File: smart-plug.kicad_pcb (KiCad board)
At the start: 2 copper layers, 58 x 53 mm, 24 parts, among them J1 Screw_Terminal_01x03, Q1 STGD5NB120SZ, Q2 BTA316B-600E, U1 ESP32-PICO-KIT, U2 SR086, U3 TPS560430X3F, U4 FODM3012

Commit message: rename project
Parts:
- D1: footprint ThinglerV05:ABS10A -> smart-plug:ABS10A
- F1: footprint ThinglerV05:Fuse -> smart-plug:Fuse
- L1: footprint ThinglerV05:ME3220 -> smart-plug:ME3220
- U1: footprint ThinglerV05:ESP32-PICO-KIT -> smart-plug:ESP32-PICO-KIT
- U4: footprint ThinglerV05:FODM3012 -> smart-plug:FODM3012
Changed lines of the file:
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@@
     (add_net "Net-(R8-Pad2)")
   )
-  (module ThinglerV05:FODM3012 (layer F.Cu)
+  (module smart-plug:FODM3012 (layer F.Cu)
     (at 168.5 70.25 180)
     (fp_text reference U4 (at 0 0) (layer F.SilkS)
@@
       (net 20 "Net-(R5-Pad1)"))
   )
-  (module ThinglerV05:ESP32-PICO-KIT (layer F.Cu)
+  (module smart-plug:ESP32-PICO-KIT (layer F.Cu)
     (at 145 86.75 90)
     (fp_text reference U1 (at 0 0 180) (layer F.SilkS)
@@
     )
   )
-  (module ThinglerV05:ME3220 (layer F.Cu)
+  (module smart-plug:ME3220 (layer F.Cu)
     (at 157.25 73)
     (fp_text reference L1 (at 0 2.75) (layer F.SilkS)
@@
     )
   )
-  (module ThinglerV05:ABS10A (layer F.Cu)
+  (module smart-plug:ABS10A (layer F.Cu)
     (at 138.5 66.25 90)
     (fp_text reference D1 (at 0 0 180) (layer F.SilkS)
@@
       (net 13 "Net-(D1-Pad4)"))
   )
-  (module ThinglerV05:Fuse (layer F.Cu)
+  (module smart-plug:Fuse (layer F.Cu)
     (at 131.75 66.25 180)
     (descr "Littelfuse, resettable fuse, PTC, polyswitch LVR100, Ih 1A http://www.littelfuse.com/~/media/electronics/datasheets/resettable_ptcs/littelfuse_ptc_lvr_catalog_datasheet.pdf.pdf")

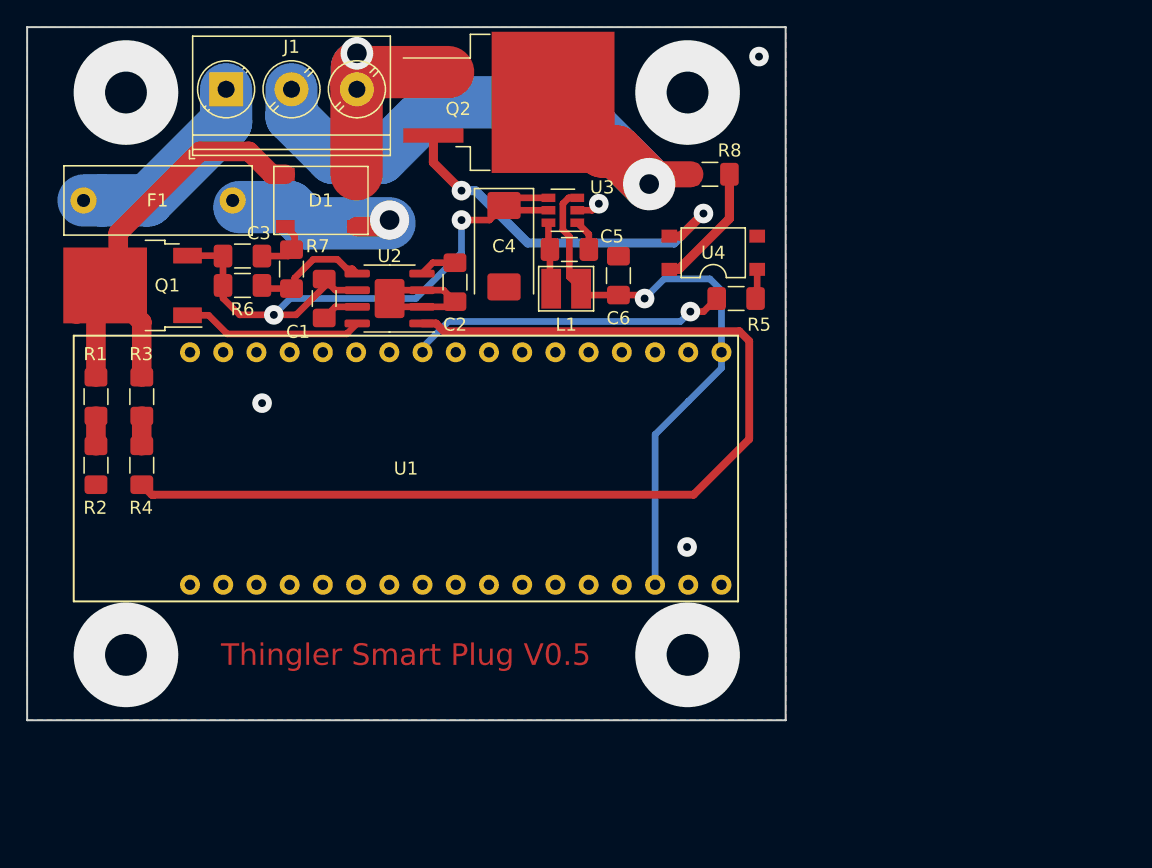
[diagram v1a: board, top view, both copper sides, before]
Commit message: pcb for voltage and current measurements
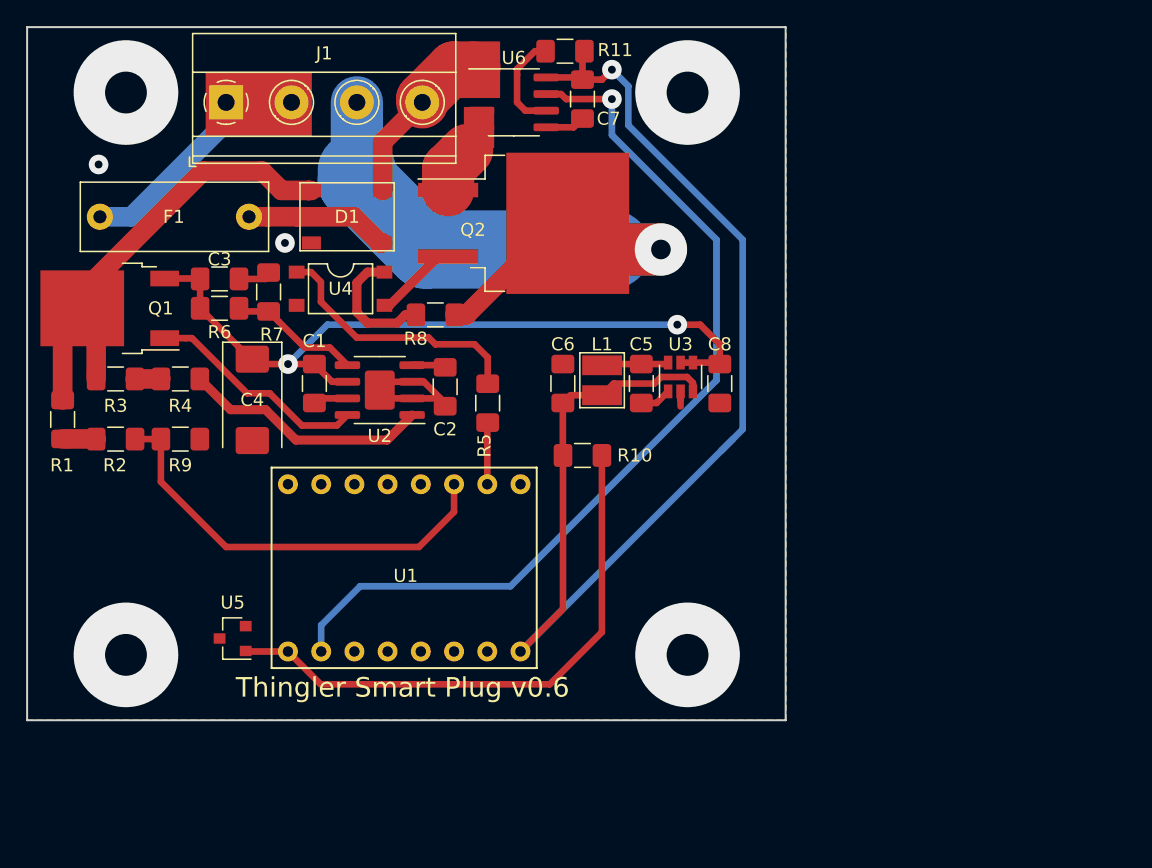
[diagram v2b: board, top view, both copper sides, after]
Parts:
- added C7: 100n, Capacitor_SMD:C_1206_3216Metric_Pad1.42x1.75mm_HandSolder, F.Cu at (158.5, 58.5)
- added C8: 100n, Capacitor_SMD:C_1206_3216Metric_Pad1.42x1.75mm_HandSolder, F.Cu at (169.0, 80.2)
- added R10: 12.4k, Resistor_SMD:R_1206_3216Metric_Pad1.42x1.75mm_HandSolder, F.Cu at (158.5, 85.8)
- added R11: 113k, Resistor_SMD:R_1206_3216Metric_Pad1.42x1.75mm_HandSolder, F.Cu at (157.2, 54.8)
- added R9: 2.4k 0.1%, Resistor_SMD:R_1206_3216Metric_Pad1.42x1.75mm_HandSolder, F.Cu at (127.8, 84.5)
- added U5: LM4041, Package_TO_SOT_SMD:SOT-23, F.Cu at (131.8, 99.8)
- added U6: ACS71240LLCBTR-030B3, Package_SO:SOIC-8_3.9x4.9mm_P1.27mm, F.Cu at (153.2, 58.8)
- J1: value Screw_Terminal_01x03 -> Screw_Terminal_01x04; footprint TerminalBlock_Phoenix:TerminalBlock_Phoenix_PT-1,5-3-5.0-H_1x03_P5.00mm_Horizontal -> TerminalBlock_Phoenix:TerminalBlock_Phoenix_MKDS-1,5-4_1x04_P5.00mm_Horizontal
- R1, R2: value 200k -> 200k 0.1%
- U1: value ESP32-PICO-KIT -> THINGLER-ESP32-PICO; footprint smart-plug:ESP32-PICO-KIT -> smart-plug:THINGLER-ESP32-PICO
- moved U4 28.6 mm to (140.0, 73.0), turned to 0 degrees
- moved R8 23.6 mm to (147.2, 75.0), turned to 180 degrees
- moved C4 22.6 mm to (133.2, 81.5)
- moved R5 20.6 mm to (151.2, 81.8), turned to 270 degrees
- moved U1 16.5 mm to (153.8, 100.8), turned to 270 degrees
- moved U3 15.6 mm to (166.0, 79.8), turned to 90 degrees
- moved C5 11.6 mm to (163.0, 80.2), turned to 90 degrees
- moved Q2 9.32 mm to (154.0, 68.0)
- moved C6 9.28 mm to (157.0, 80.2)
- moved C2 8.04 mm to (148.0, 80.5)
- moved L1 7.52 mm to (160.0, 80.0), turned to 270 degrees
- moved R4 7.23 mm to (127.8, 79.9), turned to 0 degrees
- moved U2 7.04 mm to (143.0, 80.8)
- moved C1 6.54 mm to (138.0, 80.2)
- moved R1 3.09 mm to (118.8, 83.0)
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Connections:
- J1 pad 2: Net-(J1-Pad2) -> AC
- J1 pad 3: NEUT -> Net-(J1-Pad3)
- Q2 pad 1: NEUT -> Net-(Q2-Pad1)
- Q2 pad 2: Net-(J1-Pad2) -> Net-(J1-Pad3)
- R2 pad 2: Earth -> /I37
- R8 pad 1: Net-(J1-Pad2) -> Net-(J1-Pad3)
- U1 pad 10: (no net) -> Net-(R5-Pad2)
- U1 pad 11: Net-(R5-Pad2) -> /I37
- U1 pad 7: (no net) -> /IO33
- U1 pad 8: (no net) -> Net-(R10-Pad2)
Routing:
- net /IO33: track 0.00 -> 70.0 mm, vias 0 -> 1
- net Net-(R4-Pad2): track 81.6 -> 19.0 mm
- net +3V3: track 45.0 -> 97.4 mm
- net Net-(J1-Pad3): track 0.00 -> 50.2 mm, vias 0 -> 1
- net Net-(J1-Pad2): track 47.4 -> 0.00 mm, vias 1 -> 0
- net Net-(R10-Pad2): track 0.00 -> 43.5 mm
- net /I37: track 0.00 -> 33.0 mm
- net Net-(Q2-Pad3): track 29.5 -> 5.66 mm, vias 2 -> 0
- net Net-(R5-Pad2): track 24.4 -> 4.72 mm, vias 1 -> 0
- net Net-(R5-Pad1): track 2.45 -> 20.8 mm
- net /12VDC: track 48.8 -> 58.0 mm
- net Net-(R11-Pad1): track 0.00 -> 7.77 mm
- net Net-(D1-Pad1): track 44.2 -> 36.7 mm
- net Net-(Q2-Pad1): track 0.00 -> 4.93 mm
- net Net-(D1-Pad4): track 14.7 -> 11.1 mm, vias 1 -> 0
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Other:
- board text added: "Thingler Smart Plug v0.6"
- board text removed: "Thingler Smart Plug V0.5"

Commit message: Thingler Smart Plug schematics for 3D print (#1)
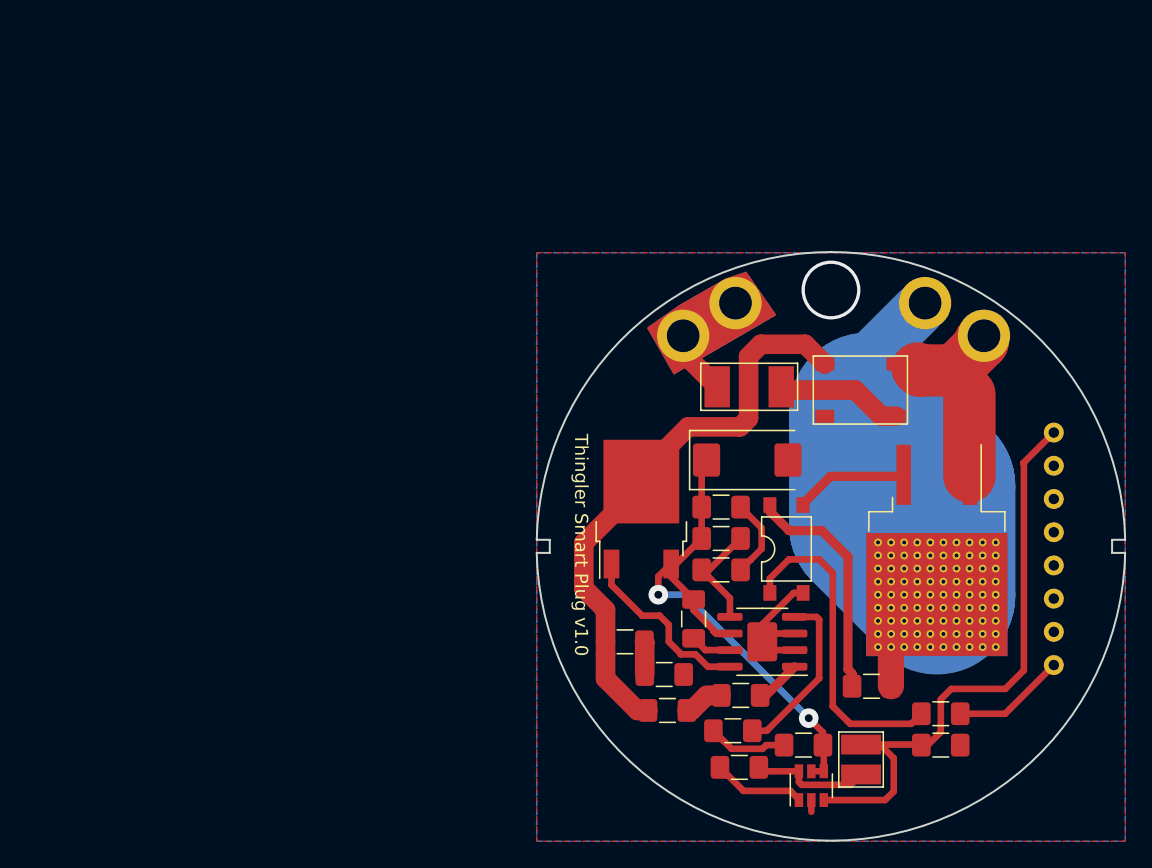
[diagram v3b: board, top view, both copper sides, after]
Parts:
- removed C8: 100n, Capacitor_SMD:C_1206_3216Metric_Pad1.42x1.75mm_HandSolder
- removed R10: 12.4k, Resistor_SMD:R_1206_3216Metric_Pad1.42x1.75mm_HandSolder
- removed R11: 113k, Resistor_SMD:R_1206_3216Metric_Pad1.42x1.75mm_HandSolder
- removed R9: 2.4k 0.1%, Resistor_SMD:R_1206_3216Metric_Pad1.42x1.75mm_HandSolder
- removed U5: LM4041, Package_TO_SOT_SMD:SOT-23
- removed U6: ACS71240LLCBTR-030B3, Package_SO:SOIC-8_3.9x4.9mm_P1.27mm
- C6: value 33u -> 100n
- C7: value 100n -> 33u
- F1: footprint smart-plug:Fuse -> smart-plug:fuse-2410
- J1: footprint TerminalBlock_Phoenix:TerminalBlock_Phoenix_MKDS-1,5-4_1x04_P5.00mm_Horizontal -> smart-plug:3d_power_connector
- Q2: footprint Package_TO_SOT_SMD:TO-263-2 -> smart-plug:to-263-2
- R1, R2: value 200k 0.1% -> 200k
- U1: footprint smart-plug:THINGLER-ESP32-PICO -> smart-plug:Thingler-esp32-vertical; moved to B.Cu
- U3: value TPS560430X3F -> FODM3012; footprint Package_TO_SOT_SMD:SOT-23-6 -> smart-plug:FODM3012
- U4: value FODM3012 -> TPS560430X3F; footprint smart-plug:FODM3012 -> Package_TO_SOT_SMD:SOT-23-6
- moved C7 56.5 mm to (185.9, 107.9), turned to 180 degrees
- moved U4 52.3 mm to (176.0, 111.0), turned to 90 degrees
- moved R3 49.2 mm to (165.0, 105.2)
- moved R4 49.2 mm to (170.6, 104.1)
- moved J1 48.9 mm to (177.7, 74.1)
- moved R1 46.2 mm to (161.8, 100.0), turned to 0 degrees
- moved R2 45.6 mm to (164.8, 102.5)
- moved U1 44.1 mm to (194.5, 84.0), turned to 180 degrees
- moved R8 43.8 mm to (180.6, 103.4)
- moved Q1 43.5 mm to (163.0, 89.8), turned to 90 degrees
- moved R6 42.2 mm to (169.1, 92.1)
- moved C3 42.1 mm to (169.1, 89.7)
- moved R5 42.0 mm to (185.9, 105.5), turned to 0 degrees
- moved D1 41.4 mm to (179.8, 80.8)
- moved R7 40.6 mm to (169.1, 94.5), turned to 180 degrees
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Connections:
- C5 pad 1: Net-(C5-Pad1) -> /12VDC
- C5 pad 2: Net-(C5-Pad2) -> Earth
- C6 pad 1: Earth -> Net-(C6-Pad1)
- C6 pad 2: +3V3 -> Net-(C6-Pad2)
- C7 pad 1: +3V3 -> Earth
- C7 pad 2: Earth -> +3V3
- L1 pad 1: Net-(C5-Pad2) -> Net-(C6-Pad2)
- Q2 pad 1: Net-(Q2-Pad1) -> NEUT
- R2 pad 2: /I37 -> Earth
- U1 pad 7: /IO33 -> (no net)
- U1 pad 8: Net-(R10-Pad2) -> Net-(R5-Pad2)
- U3 pad 1: Net-(C5-Pad1) -> Net-(R5-Pad1)
- U3 pad 3: +3V3 -> Net-(Q2-Pad3)
- U3 pad 4: /12VDC -> Net-(R8-Pad2)
- U4 pad 1: Net-(R5-Pad1) -> Net-(C6-Pad1)
- U4 pad 3: Net-(Q2-Pad3) -> +3V3
- U4 pad 4: Net-(R8-Pad2) -> /12VDC
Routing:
- net /IO33: track 70.0 -> 0.00 mm, vias 1 -> 0
- net +3V3: track 97.4 -> 46.6 mm, vias 1 -> 0
- net Net-(R10-Pad2): track 43.5 -> 0.00 mm
- net /I37: track 33.0 -> 0.00 mm
- net /12VDC: track 58.0 -> 40.8 mm
- net Net-(R4-Pad2): track 19.0 -> 3.55 mm
- net Net-(C2-Pad1): track 2.59 -> 13.2 mm
- net Net-(C6-Pad2): track 0.00 -> 9.18 mm
- net AC: track 19.2 -> 10.0 mm
- net Net-(R8-Pad2): track 9.82 -> 17.9 mm
- net Net-(R11-Pad1): track 7.77 -> 0.00 mm
- net Net-(D1-Pad1): track 36.7 -> 44.0 mm
- net Net-(C6-Pad1): track 0.00 -> 7.10 mm
- net Earth: track 18.6 -> 24.1 mm, vias 2 -> 0
- net Net-(C5-Pad2): track 5.29 -> 0.00 mm
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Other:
- board size 58 x 53 mm -> 45 x 45 mm
- net class AC230V_HIGH_POWER: trace_width 4 -> 12
- board text added: "Thingler Smart Plug v1.0"
- board text removed: "Thingler Smart Plug v0.6"

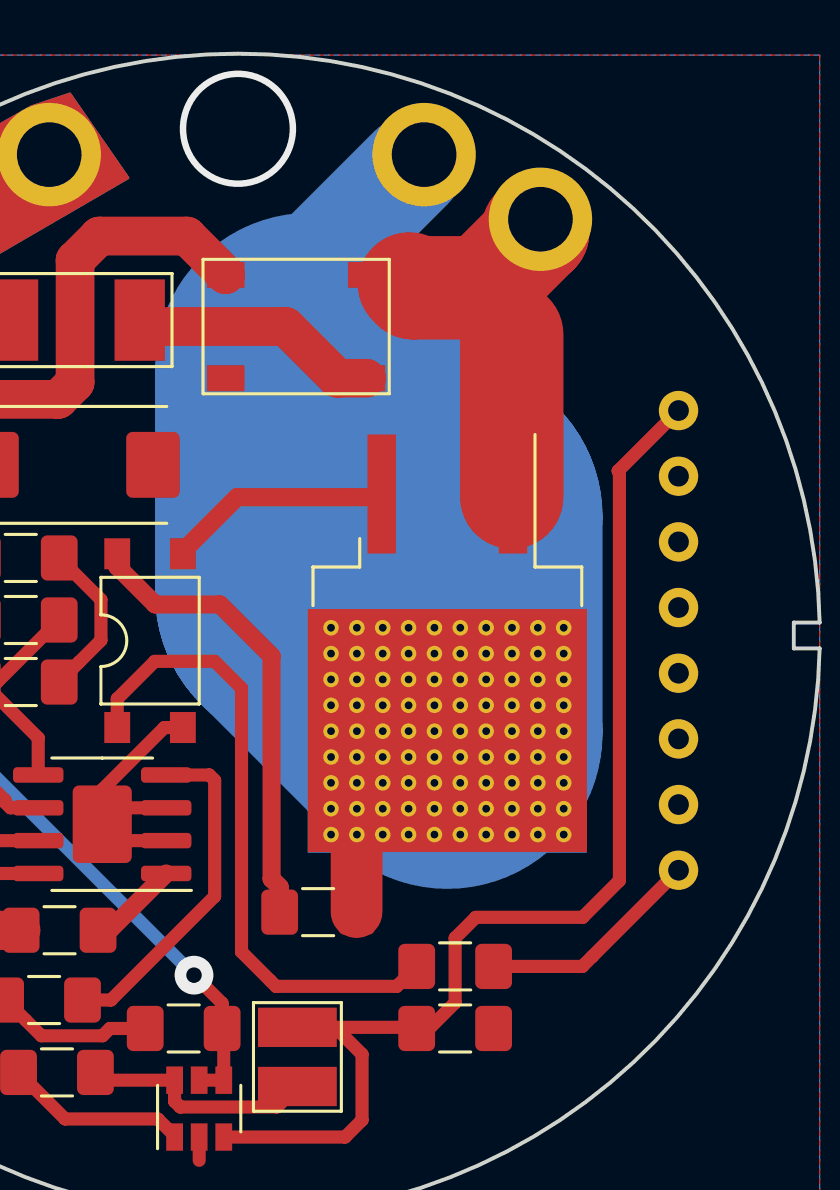
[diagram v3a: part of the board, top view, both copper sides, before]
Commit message: increased width for power traces
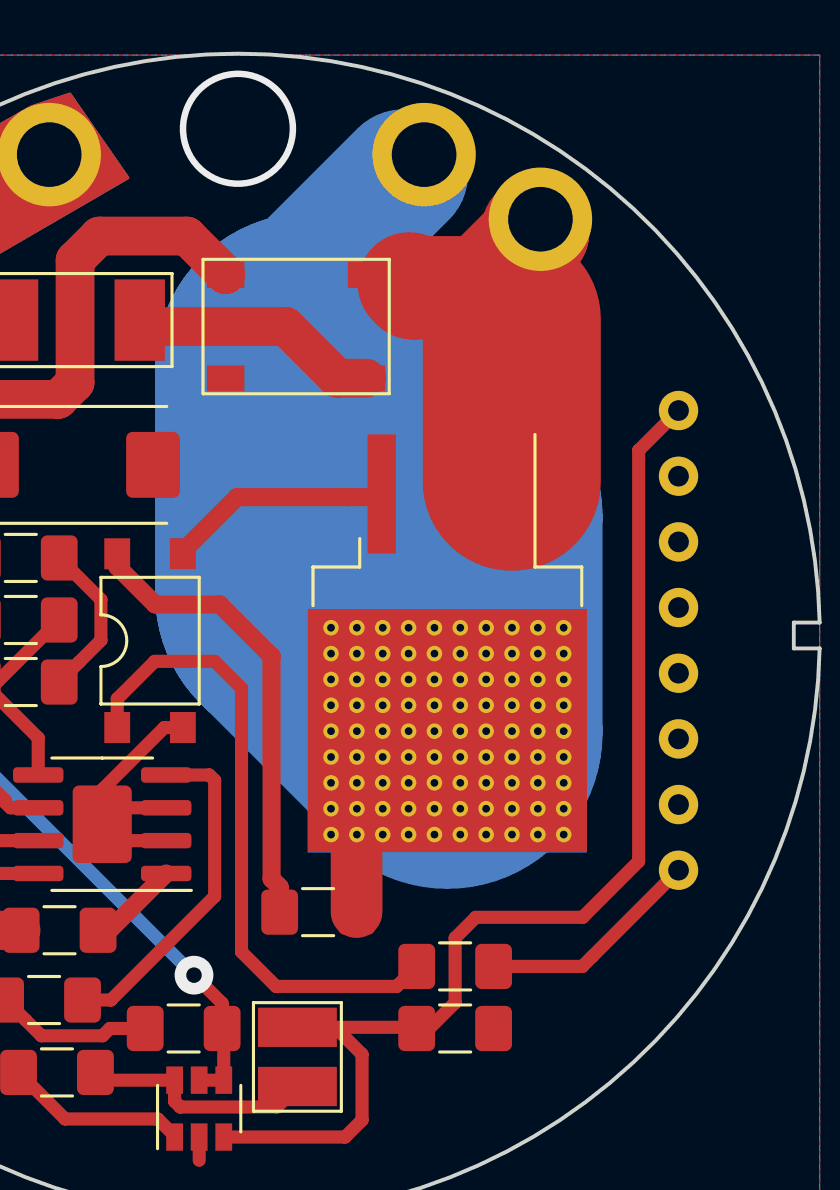
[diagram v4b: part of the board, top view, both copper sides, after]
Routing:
- net Net-(J1-Pad3): track 47.2 -> 48.6 mm
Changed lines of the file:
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@@
   (segment (start 181.644402 112.1) (end 182.3 111.444402) (width 0.508) (layer F.Cu) (net 3))
   (segment (start 176.95 112.1) (end 181.644402 112.1) (width 0.508) (layer F.Cu) (net 3) (status 10))
-  (segment (start 192.204001 86.335999) (end 194.541 83.999) (width 0.508) (layer F.Cu) (net 3) (status 20))
-  (segment (start 192.254001 86.385999) (end 192.204001 86.335999) (width 0.508) (layer F.Cu) (net 3))
-  (segment (start 192.254001 102.178201) (end 192.254001 86.385999) (width 0.508) (layer F.Cu) (net 3))
-  (segment (start 190.832202 103.6) (end 192.254001 102.178201) (width 0.508) (layer F.Cu) (net 3))
-  (segment (start 186.7 103.6) (end 190.832202 103.6) (width 0.508) (layer F.Cu) (net 3))
-  (segment (start 185.9 104.4) (end 186.7 103.6) (width 0.508) (layer F.Cu) (net 3))
-  (segment (start 185.9 106.9) (end 185.9 104.4) (width 0.508) (layer F.Cu) (net 3))
-  (segment (start 184.9 107.9) (end 185.9 106.9) (width 0.508) (layer F.Cu) (net 3) (status 10))
-  (segment (start 184.4125 107.9) (end 184.9 107.9) (width 0.508) (layer F.Cu) (net 3) (status 30))
   (segment (start 184.3675 107.855) (end 184.4125 107.9) (width 0.508) (layer F.Cu) (net 3) (status 30))
   (segment (start 179.8 107.855) (end 184.3675 107.855) (width 0.508) (layer F.Cu) (net 3) (status 30))
-  (segment (start 188.09 87.35) (end 188.09 81.05) (width 4) (layer F.Cu) (net 4))
+  (segment (start 184.9 107.9) (end 184.4125 107.9) (width 0.508) (layer F.Cu) (net 3))
+  (segment (start 185.9 106.9) (end 184.9 107.9) (width 0.508) (layer F.Cu) (net 3))
+  (segment (start 185.9 104.4) (end 185.9 106.9) (width 0.508) (layer F.Cu) (net 3))
+  (segment (start 186.7 103.6) (end 185.9 104.4) (width 0.508) (layer F.Cu) (net 3))
+  (segment (start 193 101.432202) (end 190.832202 103.6) (width 0.508) (layer F.Cu) (net 3))
+  (segment (start 190.832202 103.6) (end 186.7 103.6) (width 0.508) (layer F.Cu) (net 3))
+  (segment (start 193 85.54) (end 193 101.432202) (width 0.508) (layer F.Cu) (net 3))
+  (segment (start 194.541 83.999) (end 193 85.54) (width 0.508) (layer F.Cu) (net 3))
+  (segment (start 188.09 86.75) (end 188.09 80.45) (width 6.89) (layer F.Cu) (net 4))
   (segment (start 184.278314 79.249999) (end 184.128316 79.100001) (width 4) (layer F.Cu) (net 4))
   (segment (start 189.092955 77.107048) (end 188.920418 76.980158) (width 4) (layer F.Cu) (net 4) (status 30))
@@
   (segment (start 184.4125 105.5) (end 183.641153 106.271347) (width 0.508) (layer F.Cu) (net 17) (status 10))
   (segment (start 178.75 106.05) (end 177.63799 104.93799) (width 0.508) (layer F.Cu) (net 17))
-  (segment (start 172.83 90.03) (end 172.83 89.54) (width 0.7) (layer F.Cu) (net 18) (status 30))
+  (segment (start 179.1125 102.425) (end 178.8 102.1125) (width 0.7) (layer F.Cu) (net 18))
+  (segment (start 179.1125 103.4) (end 179.1125 102.425) (width 0.7) (layer F.Cu) (net 18) (status 10))
+  (segment (start 176.8 91.5) (end 174.3 91.5) (width 0.7) (layer F.Cu) (net 18))
   (segment (start 174.3 91.5) (end 172.83 90.03) (width 0.7) (layer F.Cu) (net 18) (status 20))
   (segment (start 178.8 93.5) (end 176.8 91.5) (width 0.7) (layer F.Cu) (net 18))
+  (segment (start 172.83 90.03) (end 172.83 89.54) (width 0.7) (layer F.Cu) (net 18) (status 30))
   (segment (start 178.8 102.1125) (end 178.8 93.5) (width 0.7) (layer F.Cu) (net 18))
-  (segment (start 179.1125 102.425) (end 178.8 102.1125) (width 0.7) (layer F.Cu) (net 18))
-  (segment (start 176.8 91.5) (end 174.3 91.5) (width 0.7) (layer F.Cu) (net 18))
-  (segment (start 179.1125 103.4) (end 179.1125 102.425) (width 0.7) (layer F.Cu) (net 18) (status 10))
-  (segment (start 180.295998 78.504002) (end 184.199999 74.600002) (width 4) (layer B.Cu) (net 19) (status 20))
+  (segment (start 180 78.75) (end 183.904001 74.846) (width 5) (layer B.Cu) (net 19) (status 20))
   (segment (start 180.295998 82.795998) (end 180.295998 82.350001) (width 12) (layer B.Cu) (net 19))
   (segment (start 185.6 88.1) (end 180.295998 82.795998) (width 12) (layer B.Cu) (net 19))
@@
   (segment (start 180.295998 91.095998) (end 185.6 96.4) (width 12) (layer B.Cu) (net 19))
   (segment (start 180.295998 82.795998) (end 180.295998 91.095998) (width 12) (layer B.Cu) (net 19))
+  (segment (start 180.295998 82.350001) (end 181.629999 82.350001) (width 12) (layer B.Cu) (net 19))
   (segment (start 172.2875 109.9) (end 171.9875 109.6) (width 0.508) (layer F.Cu) (net 20) (status 30))
   (segment (start 175.05 109.9) (end 172.2875 109.9) (width 0.508) (layer F.Cu) (net 20) (status 30))
